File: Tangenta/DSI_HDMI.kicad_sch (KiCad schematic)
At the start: 30 parts, among them J8 HDMI_19PIN_043, U13 LT8912B

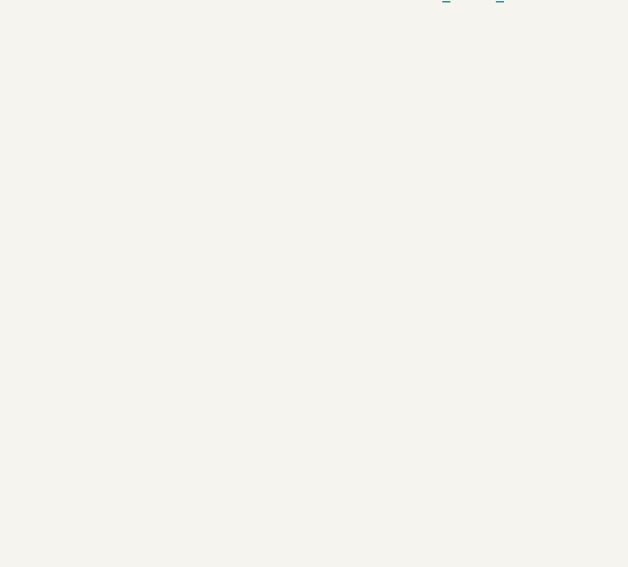
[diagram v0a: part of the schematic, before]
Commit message: Adding 25MHz oscillator.
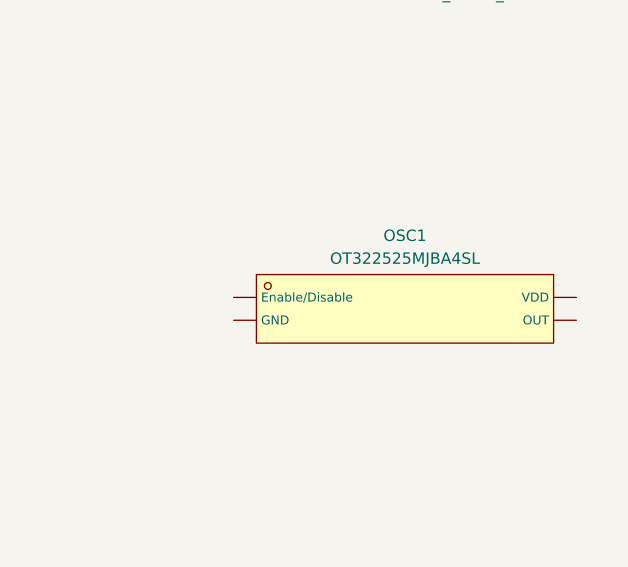
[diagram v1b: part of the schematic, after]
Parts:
- added OSC1: OT322525MJBA4SL, 25MHZ_OSCILLATOR:25MHZ_OSCILLATOR, symbol 25MHZ_OSCILLATOR:OT322525MJBA4SL
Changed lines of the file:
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@@
+    )
+  )
+  (symbol (lib_id "25MHZ_OSCILLATOR:OT322525MJBA4SL") (at 376.809 110.998 0) (unit 1)
+    (in_bom yes) (on_board yes) (dnp no) (fields_autoplaced)
+    (property "Reference" "OSC1" (at 376.809 102.87 0)
+      (effects (font (size 1.27 1.27)))
+    )
+    (property "Value" "OT322525MJBA4SL" (at 376.809 105.41 0)
+      (effects (font (size 1.27 1.27)))
+    )
+    (property "Footprint" "25MHZ_OSCILLATOR:25MHZ_OSCILLATOR" (at 378.333 123.063 0)
+      (effects (font (size 1.27 1.27) italic) hide)
+    )
+    (property "Datasheet" "https://item.szlcsc.com/15866.html" (at 359.791 121.031 0)
+      (effects (font (size 1.27 1.27)) (justify left) hide)
+    )
+    (property "LCSC" "C669088" (at 364.236 119.126 0)
+      (effects (font (size 1.27 1.27)) hide)
+    )
+    (pin "1")
+    (pin "2")
+    (pin "3")
+    (pin "4")
+    (instances
+      (project "Tangenta"
+        (path "/358d1bcf-7599-4352-8c4d-baa18a5f09e6/6a8c68b5-4a7d-449e-86f6-34ced6d1cb55"
+          (reference "OSC1") (unit 1)
+        )
+      )
     )
   )

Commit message: Lontium - current progress...
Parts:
- added C1: 2.2nF, Capacitor_SMD:C_0402_1005Metric, symbol Device:C_Small
- added R2: 100k, Resistor_SMD:R_0402_1005Metric, symbol Device:R_Small_US
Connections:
- net DSI.CLK_N: now also U13.8 (MIPIRX_CKN)
- net DSI.CLK_P: now also U13.7 (MIPIRX_CKP)
- net DSI.D0_N: now also U13.2 (MIPIRX0_DN)
- net DSI.D0_P: now also U13.1 (MIPIRX0_DP)
- net DSI.D1_N: now also U13.4 (MIPIRX1_DN)
- net DSI.D1_P: now also U13.3 (MIPIRX1_DP)
- net DSI.D2_N: now also U13.10 (MIPIRX2_DN)
- net DSI.D2_P: now also U13.9 (MIPIRX2_DP)
- net DSI.D3_N: now also U13.12 (MIPIRX3_DN)
- net DSI.D3_P: now also U13.11 (MIPIRX3_DP)
- net DSI.HPD: now also U13.14 (HPD)
- net DSI.INT: now also U13.63 (INT), R2.2
- net DSI.nRST: now also U13.64 (RESET_N)
- net GNDREF: now also R2.1
- net VCCA_HDMIPLL: now also U13.34 (VCCA_HDMIPLL), C1.1
- net VCCA_HDMITX: now also U13.26 (VCCA_HDMITX)
- net VCCA_LVDSPLL: now also U13.52 (VCCA_LVDSPLL)
- net VCCA_LVDSTX: now also U13.41 (VCCA_LVDSTX)
- net VCCA_MIPIRX: now also U13.5 (VCCA_MIPIRX)
- net VCCA_SYSCLK: now also U13.50 (VCCA_SYSCLK)
- net VDD: now also U13.18 (VDD), U13.33 (VDD), U13.57 (VDD)
- net at U13.35 (LPF): now also C1.2
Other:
- moved on the sheet: J8, OSC1

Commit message: DSI_HDMI current progress...
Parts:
- added C1: 10nF, Capacitor_SMD:C_0402_1005Metric, symbol Device:C_Small
- added C1: 10uF, Capacitor_SMD:C_0402_1005Metric, symbol Device:C_Small
- added C1: 100nF, Capacitor_SMD:C_0402_1005Metric, symbol Device:C_Small
- added FB1: GZ2012D101TF, Ferrite_Bead_100:Ferrite_Bead_100, symbol Ferrite_Bead_100:GZ2012D101TF
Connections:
- net 1V8: now also FB1.1
- net GNDREF: now also OSC1.2 (GND), C1.1, C1.1, C1.1
- net XTALI: now reaches U13.53 (XTALI)
- net XTALI: now also OSC1.3 (OUT)
- net I2S.D_OUT: now reaches U13.58 (SD0_CEC)
- net I2S.SYNC: now reaches U13.59 (WS_I)
- net I2S.BCLK: now reaches U13.60 (SCLK_I)
- net at OSC1.1 (Enable/Disable): now also OSC1.4 (VDD), C1.2, C1.2, C1.2, FB1.2
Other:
- moved on the sheet: OSC1

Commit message: Current progress...
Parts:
- added R2 (x2): 1.8k, Resistor_SMD:R_0402_1005Metric, symbol Device:R_Small_US
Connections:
- net 1V8: now also R2.2, R2.2
- net I2C.SDA: now reaches U13.61 (S_SDA)
- net I2C.SDA: now also R2.1
- net I2C.SCL: now reaches U13.62 (S_SCL)
- net I2C.SCL: now also R2.1
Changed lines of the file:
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@@
   (junction (at 124.46 248.92) (diameter 0) (color 0 0 0 0)
   )
+  (junction (at 44.45 203.2) (diameter 0) (color 0 0 0 0)
+  )
   (junction (at 88.9 267.97) (diameter 0) (color 0 0 0 0)
   )
+  (junction (at 55.88 207.01) (diameter 0) (color 0 0 0 0)
+  )
   (junction (at 53.34 181.61) (diameter 0) (color 0 0 0 0)
   )
@@
     (stroke (width 0) (type default))
   )
+  (bus_entry (at 111.76 92.71) (size 2.54 -2.54)
+    (stroke (width 0) (type default))
+  )
+  (bus_entry (at 111.76 95.25) (size 2.54 -2.54)
+    (stroke (width 0) (type default))
+  )
   (bus_entry (at 111.76 41.91) (size 2.54 -2.54)
     (stroke (width 0) (type default))
@@
     (stroke (width 0) (type default))
   )
+  (wire (pts (xy 20.32 203.2) (xy 44.45 203.2))
+    (stroke (width 0) (type default))
+  )
   (wire (pts (xy 242.57 114.3) (xy 242.57 116.84))
     (stroke (width 0) (type default))
@@
     (stroke (width 0) (type default))
   )
+  (wire (pts (xy 44.45 190.5) (xy 44.45 194.31))
+    (stroke (width 0) (type default))
+  )
   (wire (pts (xy 62.23 226.06) (xy 62.23 229.87))
     (stroke (width 0) (type default))
@@
     (stroke (width 0) (type default))
   )
+  (wire (pts (xy 114.3 90.17) (xy 130.81 90.17))
+    (stroke (width 0) (type default))
+  )
   (wire (pts (xy 46.99 229.87) (xy 46.99 226.06))
     (stroke (width 0) (type default))
@@
     (stroke (width 0) (type default))
   )
+  (wire (pts (xy 246.38 44.45) (xy 229.87 44.45))
+    (stroke (width 0) (type default))
+  )
   (wire (pts (xy 143.51 125.73) (xy 127 125.73))
     (stroke (width 0) (type default))
@@
     (stroke (width 0) (type default))
   )
+  (wire (pts (xy 246.38 41.91) (xy 229.87 41.91))
+    (stroke (width 0) (type default))
+  )
   (wire (pts (xy 114.3 78.74) (xy 130.81 78.74))
     (stroke (width 0) (type default))
@@
     (stroke (width 0) (type default))
   )
+  (bus (pts (xy 111.76 95.25) (xy 111.76 101.6))
+    (stroke (width 0) (type default))
+  )
   (wire (pts (xy 46.99 260.35) (xy 54.61 260.35))
     (stroke (width 0) (type default))
@@
     (stroke (width 0) (type default))
   )
+  (wire (pts (xy 114.3 92.71) (xy 130.81 92.71))
+    (stroke (width 0) (type default))
+  )
   (wire (pts (xy 60.96 175.26) (xy 59.69 175.26))
     (stroke (width 0) (type default))
@@
     (stroke (width 0) (type default))
   )
+  (wire (pts (xy 55.88 194.31) (xy 55.88 190.5))
+    (stroke (width 0) (type default))
+  )
   (wire (pts (xy 40.64 181.61) (xy 46.99 181.61))
     (stroke (width 0) (type default))
@@
     (stroke (width 0) (type default))
   )
+  (bus (pts (xy 100.33 101.6) (xy 111.76 101.6))
+    (stroke (width 0) (type default))
+  )
   (bus (pts (xy 111.76 78.74) (xy 111.76 81.28))
     (stroke (width 0) (type default))
@@
     (stroke (width 0) (type default))
   )
+  (wire (pts (xy 20.32 207.01) (xy 55.88 207.01))
+    (stroke (width 0) (type default))
+  )
   (wire (pts (xy 62.23 236.22) (xy 62.23 233.68))
     (stroke (width 0) (type default))
@@
     (stroke (width 0) (type default))
   )
+  (wire (pts (xy 44.45 203.2) (xy 67.31 203.2))
+    (stroke (width 0) (type default))
+  )
   (wire (pts (xy 54.61 241.3) (xy 54.61 245.11))
     (stroke (width 0) (type default))
@@
     (stroke (width 0) (type default))
   )
+  (wire (pts (xy 55.88 190.5) (xy 44.45 190.5))
+    (stroke (width 0) (type default))
+  )
   (wire (pts (xy 59.69 175.26) (xy 59.69 181.61))
     (stroke (width 0) (type default))
@@
     (stroke (width 0) (type default))
   )
+  (wire (pts (xy 44.45 199.39) (xy 44.45 203.2))
+    (stroke (width 0) (type default))
+  )
   (wire (pts (xy 179.07 127) (xy 195.58 127))
     (stroke (width 0) (type default))
@@
     (stroke (width 0) (type default))
   )
+  (wire (pts (xy 55.88 199.39) (xy 55.88 207.01))
+    (stroke (width 0) (type default))
+  )
   (wire (pts (xy 53.34 166.37) (xy 53.34 171.45))
     (stroke (width 0) (type default))
@@
     (stroke (width 0) (type default))
   )
+  (wire (pts (xy 55.88 207.01) (xy 67.31 207.01))
+    (stroke (width 0) (type default))
+  )
   (wire (pts (xy 99.06 175.26) (xy 109.22 175.26))
     (stroke (width 0) (type default))
@@
     (stroke (width 0) (type default))
   )
+  (bus (pts (xy 111.76 92.71) (xy 111.76 95.25))
+    (stroke (width 0) (type default))
+  )
   (wire (pts (xy 116.84 233.68) (xy 109.22 233.68))
     (stroke (width 0) (type default))
@@
     (effects (font (size 1.27 1.27)) (justify right bottom))
   )
+  (label "I2C.SCL" (at 20.32 207.01 0) (fields_autoplaced)
+    (effects (font (size 1.27 1.27)) (justify left bottom))
+  )
+  (label "1V8" (at 48.26 190.5 0) (fields_autoplaced)
+    (effects (font (size 1.27 1.27)) (justify left bottom))
+  )
   (label "GND" (at 81.28 279.4 0) (fields_autoplaced)
     (effects (font (size 1.27 1.27)) (justify left bottom))
@@
     (effects (font (size 1.27 1.27)) (justify left bottom))
   )
+  (label "I2C.SDA" (at 130.81 90.17 180) (fields_autoplaced)
+    (effects (font (size 1.27 1.27)) (justify right bottom))
+  )
   (label "DSI.D1_P" (at 127 128.27 0) (fields_autoplaced)
     (effects (font (size 1.27 1.27)) (justify left bottom))
@@
     (effects (font (size 1.27 1.27)) (justify left bottom))
   )
+  (label "I2C.SDA" (at 20.32 203.2 0) (fields_autoplaced)
+    (effects (font (size 1.27 1.27)) (justify left bottom))
+  )
   (label "DSI.D3_P" (at 127 143.51 0) (fields_autoplaced)
     (effects (font (size 1.27 1.27)) (justify left bottom))
@@
     (effects (font (size 1.27 1.27)) (justify left bottom))
   )
+  (label "I2C.SCL" (at 229.87 44.45 0) (fields_autoplaced)
+    (effects (font (size 1.27 1.27)) (justify left bottom))
+  )
   (label "DSI.D2_N" (at 130.81 33.02 180) (fields_autoplaced)
     (effects (font (size 1.27 1.27)) (justify right bottom))
@@
     (effects (font (size 1.27 1.27)) (justify left bottom))
   )
+  (label "I2C.SDA" (at 229.87 41.91 0) (fields_autoplaced)
+    (effects (font (size 1.27 1.27)) (justify left bottom))
+  )
   (label "VCCA_HDMIPLL" (at 77.47 218.44 180) (fields_autoplaced)
     (effects (font (size 1.27 1.27)) (justify right bottom))
@@
   )
   (label "DSI.CLK_P" (at 130.81 48.26 180) (fields_autoplaced)
+    (effects (font (size 1.27 1.27)) (justify right bottom))
+  )
+  (label "I2C.SCL" (at 130.81 92.71 180) (fields_autoplaced)
     (effects (font (size 1.27 1.27)) (justify right bottom))
   )
@@
   )
   (hierarchical_label "GND" (shape bidirectional) (at 26.67 53.34 180) (fields_autoplaced)
+    (effects (font (size 1.27 1.27)) (justify right))
+  )
+  (hierarchical_label "I2C{SDA SCL}" (shape input) (at 100.33 101.6 180) (fields_autoplaced)
     (effects (font (size 1.27 1.27)) (justify right))
   )
@@
     )
   )
+  (symbol (lib_id "Device:R_Small_US") (at 44.45 196.85 180) (unit 1)
+    (in_bom yes) (on_board yes) (dnp no)
+    (property "Reference" "R2" (at 43.18 195.58 0)
+      (effects (font (size 1.27 1.27)) (justify left))
+    )
+    (property "Value" "1.8k" (at 43.18 198.12 0)
+      (effects (font (size 1.27 1.27)) (justify left))
+    )
+    (property "Footprint" "Resistor_SMD:R_0402_1005Metric" (at 44.45 196.85 0)
+      (effects (font (size 1.27 1.27)) hide)
+    )
+    (property "Datasheet" "~" (at 44.45 196.85 0)
+      (effects (font (size 1.27 1.27)) hide)
+    )
+    (pin "1")
+    (pin "2")
+    (instances
+      (project "Tangenta"
+        (path "/358d1bcf-7599-4352-8c4d-baa18a5f09e6/8215796b-9611-4f43-bcc5-319f8414b8a6"
+          (reference "R2") (unit 1)
+        )
+        (path "/358d1bcf-7599-4352-8c4d-baa18a5f09e6/d6c05402-162e-441f-bed8-be7996260fb4"
+          (reference "R18") (unit 1)
+        )
+        (path "/358d1bcf-7599-4352-8c4d-baa18a5f09e6/b1871a4d-6a35-44e2-a9a2-9a4af684371d"
+          (reference "R26") (unit 1)
+        )
+        (path "/358d1bcf-7599-4352-8c4d-baa18a5f09e6/6a8c68b5-4a7d-449e-86f6-34ced6d1cb55"
+          (reference "R41") (unit 1)
+        )
+      )
+    )
+  )
   (symbol (lib_id "Device:C_Small") (at 109.22 238.76 180) (unit 1)
     (in_bom yes) (on_board yes) (dnp no)
@@
         )
       )
+    )
+  )
+  (symbol (lib_id "Device:R_Small_US") (at 55.88 196.85 180) (unit 1)
+    (in_bom yes) (on_board yes) (dnp no)
+    (property "Reference" "R2" (at 54.61 195.58 0)
+      (effects (font (size 1.27 1.27)) (justify left))
+    )
+    (property "Value" "1.8k" (at 54.61 198.12 0)
+      (effects (font (size 1.27 1.27)) (justify left))
+    )
+    (property "Footprint" "Resistor_SMD:R_0402_1005Metric" (at 55.88 196.85 0)
+      (effects (font (size 1.27 1.27)) hide)
+    )
+    (property "Datasheet" "~" (at 55.88 196.85 0)
+      (effects (font (size 1.27 1.27)) hide)
+    )
+    (pin "1")
+    (pin "2")
+    (instances
+      (project "Tangenta"
+        (path "/358d1bcf-7599-4352-8c4d-baa18a5f09e6/8215796b-9611-4f43-bcc5-319f8414b8a6"
+          (reference "R2") (unit 1)
+        )
+        (path "/358d1bcf-7599-4352-8c4d-baa18a5f09e6/d6c05402-162e-441f-bed8-be7996260fb4"
+          (reference "R18") (unit 1)
+        )
+        (path "/358d1bcf-7599-4352-8c4d-baa18a5f09e6/b1871a4d-6a35-44e2-a9a2-9a4af684371d"
+          (reference "R26") (unit 1)
+        )
+        (path "/358d1bcf-7599-4352-8c4d-baa18a5f09e6/6a8c68b5-4a7d-449e-86f6-34ced6d1cb55"
+          (reference "R42") (unit 1)
+        )
+      )

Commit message: ...
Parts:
- added R2: 6k, Resistor_SMD:R_0402_1005Metric, symbol Device:R_Small_US
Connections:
- net GNDREF: now also U13.17 (VSS), U13.23 (VSSA_HDMITX), U13.29 (VSSA_HDMITX), U13.32 (VSS), U13.36 (VSSA_HDMIPLL), U13.42 (VSSA_LVDSTX), U13.49 (VSSA_SYSCLK), U13.51 (VSSA_LVDSPLL), U13.55 (REFCLK), U13.56 (VSS), U13.6 (VSSA_MIPIRX), U13.65 (EPAD), R2.1
- net XTALI: now also U13.53 (XTALI); no longer U13.53 (XTALI)
- net at U13.13 (R6K): now also R2.2
- no-connect marks 0 -> 15
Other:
- moved on the sheet: J8

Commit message: ...
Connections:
- net I2C.SCL renamed I2C_1.SCL
- net I2C.SDA renamed I2C_1.SDA
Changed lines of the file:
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@@
+    (stroke (width 0) (type default))
+  )
+  (bus_entry (at 111.76 109.22) (size 2.54 -2.54)
+    (stroke (width 0) (type default))
+  )
+  (bus_entry (at 111.76 111.76) (size 2.54 -2.54)
     (stroke (width 0) (type default))
   )
@@
     (stroke (width 0) (type default))
   )
+  (wire (pts (xy 114.3 106.68) (xy 130.81 106.68))
+    (stroke (width 0) (type default))
+  )
   (wire (pts (xy 35.56 248.92) (xy 46.99 248.92))
     (stroke (width 0) (type default))
@@
     (stroke (width 0) (type default))
   )
+  (wire (pts (xy 114.3 109.22) (xy 130.81 109.22))
+    (stroke (width 0) (type default))
+  )
   (wire (pts (xy 40.64 166.37) (xy 40.64 171.45))
     (stroke (width 0) (type default))
@@
     (stroke (width 0) (type default))
   )
+  (bus (pts (xy 111.76 109.22) (xy 111.76 111.76))
+    (stroke (width 0) (type default))
+  )
   (wire (pts (xy 281.94 133.35) (xy 298.45 133.35))
     (stroke (width 0) (type default))
   )
+  (bus (pts (xy 111.76 111.76) (xy 111.76 118.11))
+    (stroke (width 0) (type default))
+  )
   (wire (pts (xy 281.94 39.37) (xy 298.45 39.37))
     (stroke (width 0) (type default))
@@
     (stroke (width 0) (type default))
   )
+  (bus (pts (xy 100.33 118.11) (xy 111.76 118.11))
+    (stroke (width 0) (type default))
+  )
   (wire (pts (xy 46.99 176.53) (xy 46.99 181.61))
     (stroke (width 0) (type default))
@@
     (effects (font (size 1.27 1.27)) (justify left bottom))
   )
+  (label "I2C_2_DSI.SDA" (at 130.81 106.68 180) (fields_autoplaced)
+    (effects (font (size 1.27 1.27)) (justify right bottom))
+  )
   (label "VCCA_SYSCLK" (at 229.87 129.54 0) (fields_autoplaced)
     (effects (font (size 1.27 1.27)) (justify left bottom))
@@
     (effects (font (size 1.27 1.27)) (justify right bottom))
   )
-  (label "I2C.SCL" (at 20.32 207.01 0) (fields_autoplaced)
+  (label "I2C_1.SCL" (at 20.32 207.01 0) (fields_autoplaced)
     (effects (font (size 1.27 1.27)) (justify left bottom))
   )
@@
     (effects (font (size 1.27 1.27)) (justify left bottom))
   )
-  (label "I2C.SDA" (at 130.81 90.17 180) (fields_autoplaced)
+  (label "I2C_1.SDA" (at 130.81 90.17 180) (fields_autoplaced)
     (effects (font (size 1.27 1.27)) (justify right bottom))
   )
@@
     (effects (font (size 1.27 1.27)) (justify left bottom))
   )
+  (label "I2C_2_DSI.SCL" (at 130.81 109.22 180) (fields_autoplaced)
+    (effects (font (size 1.27 1.27)) (justify right bottom))
+  )
   (label "GND" (at 298.45 130.81 180) (fields_autoplaced)
     (effects (font (size 1.27 1.27)) (justify right bottom))
@@
     (effects (font (size 1.27 1.27)) (justify right bottom))
   )
-  (label "I2C.SDA" (at 20.32 203.2 0) (fields_autoplaced)
+  (label "I2C_1.SDA" (at 20.32 203.2 0) (fields_autoplaced)
     (effects (font (size 1.27 1.27)) (justify left bottom))
   )
@@
     (effects (font (size 1.27 1.27)) (justify left bottom))
   )
-  (label "I2C.SCL" (at 229.87 44.45 0) (fields_autoplaced)
+  (label "I2C_1.SCL" (at 229.87 44.45 0) (fields_autoplaced)
     (effects (font (size 1.27 1.27)) (justify left bottom))
   )
@@
     (effects (font (size 1.27 1.27)) (justify left bottom))
   )
-  (label "I2C.SDA" (at 229.87 41.91 0) (fields_autoplaced)
+  (label "I2C_1.SDA" (at 229.87 41.91 0) (fields_autoplaced)
     (effects (font (size 1.27 1.27)) (justify left bottom))
   )
@@
     (effects (font (size 1.27 1.27)) (justify right bottom))
   )
-  (label "I2C.SCL" (at 130.81 92.71 180) (fields_autoplaced)
+  (label "I2C_1.SCL" (at 130.81 92.71 180) (fields_autoplaced)
     (effects (font (size 1.27 1.27)) (justify right bottom))
   )
@@
   (label "GND" (at 298.45 138.43 180) (fields_autoplaced)
     (effects (font (size 1.27 1.27)) (justify right bottom))
+  )
+  (hierarchical_label "I2C_2_DSI{SDA SCL}" (shape input) (at 100.33 118.11 180) (fields_autoplaced)
+    (effects (font (size 1.27 1.27)) (justify right))
   )
   (hierarchical_label "I2S{BCLK SYNC D_OUT}" (shape input) (at 100.33 85.09 180) (fields_autoplaced)
@@
     (effects (font (size 1.27 1.27)) (justify right))
   )
-  (hierarchical_label "I2C{SDA SCL}" (shape input) (at 100.33 101.6 180) (fields_autoplaced)
+  (hierarchical_label "I2C_1{SDA SCL}" (shape input) (at 100.33 101.6 180) (fields_autoplaced)
     (effects (font (size 1.27 1.27)) (justify right))
   )
